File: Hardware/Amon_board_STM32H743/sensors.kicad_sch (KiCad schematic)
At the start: 45 parts, among them J10 GTFP08131Y2HR, J11 Conn_01x03_Male, J12 Conn_01x06_Male, J13 Conn_01x04_Male, J14 Conn_01x04_Male, J15 Conn_01x06_Male, J6 Conn_02x04_Odd_Even, J7 Red leds, J8 White leds, J9 Conn_02x04_Odd_Even, M1 Servo_X+, M2 Servo_X-, M3 Servo_Y+, M4 Servo_Y-, Q1 BC817, Q2 BC817, U6 MPU-6050, U7 BME280, U8 HMC5883L

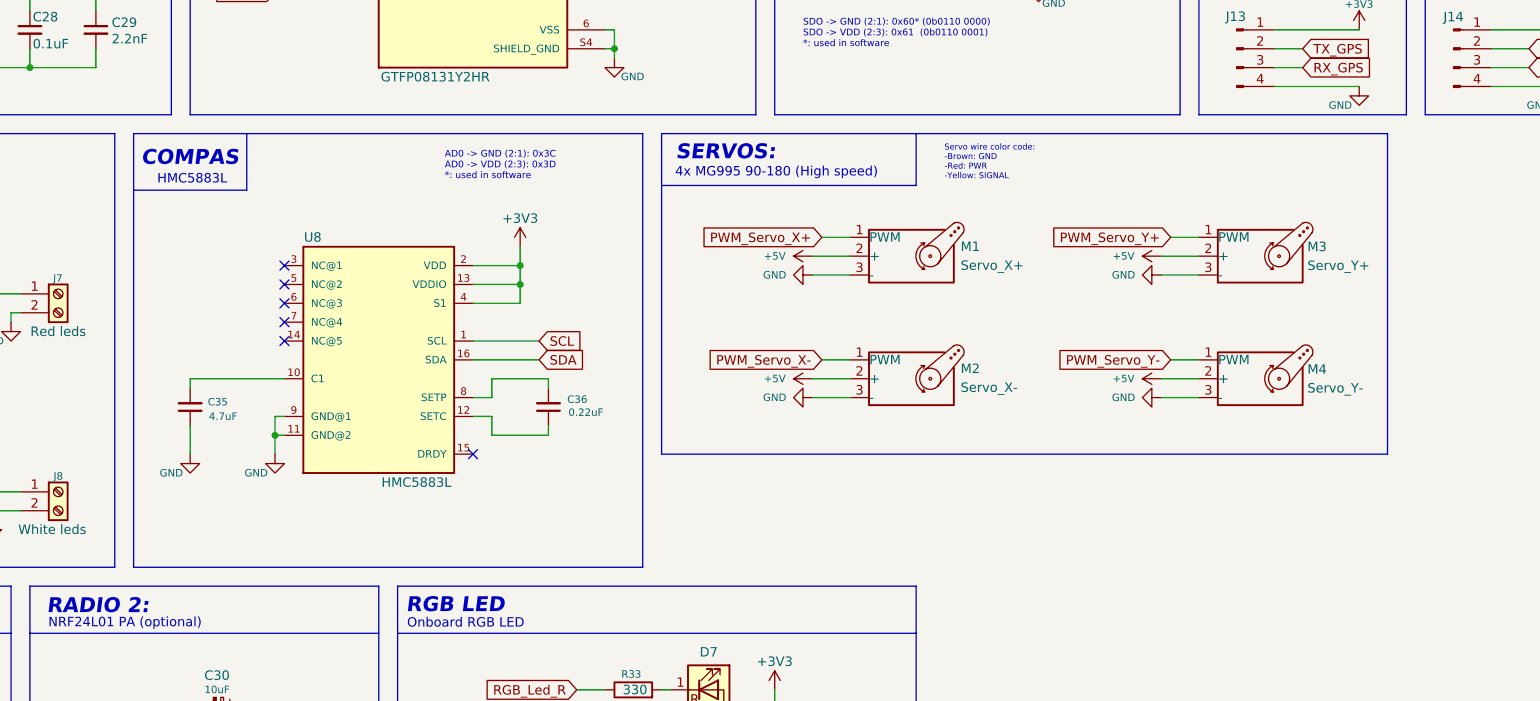
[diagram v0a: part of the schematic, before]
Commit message: Update
compas driver - untested
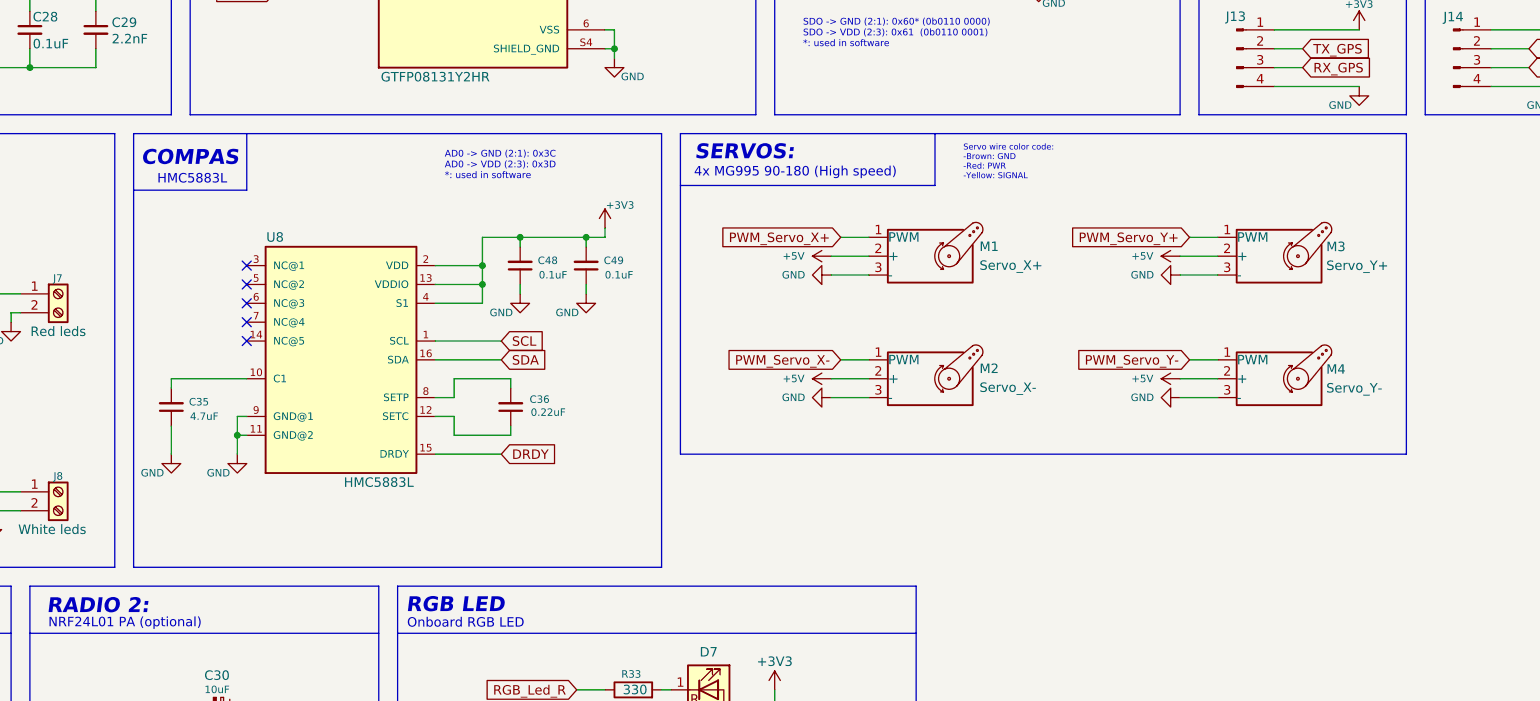
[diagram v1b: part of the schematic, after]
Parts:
- added C48, C49: 0.1uF, Capacitor_SMD:C_0603_1608Metric, symbol Device:C_Small
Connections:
- net +3V3: now also C48.2, C49.2
- net GND: now also C48.1, C49.1
- net DRDY: now reaches U8.15 (DRDY)
- no-connect marks 16 -> 15
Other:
- moved on the sheet: C35, C36, M1, M2, M3, M4, U8
